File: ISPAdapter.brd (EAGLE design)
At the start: 68 x 38 mm, 5 parts

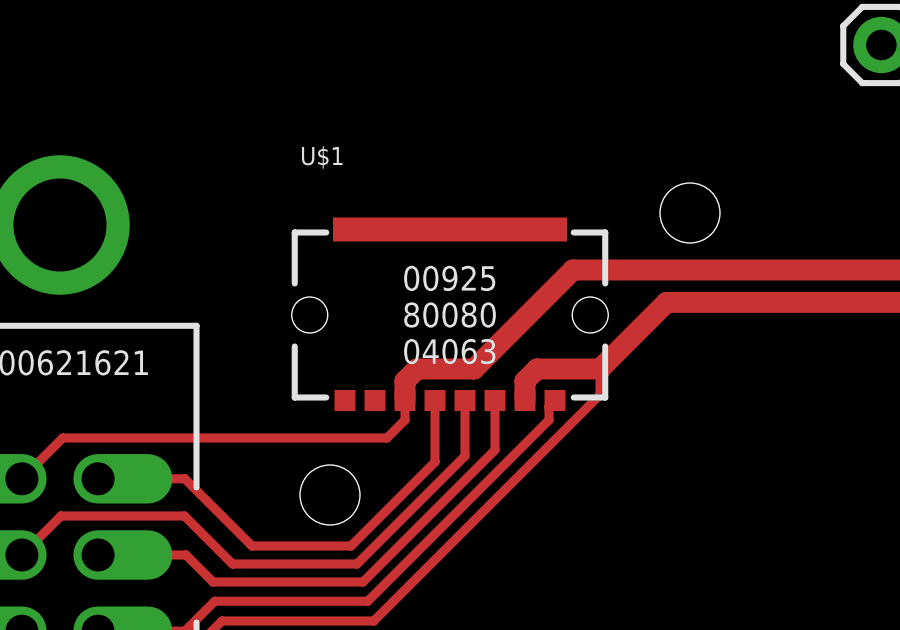
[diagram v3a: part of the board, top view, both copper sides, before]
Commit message: Added PB3 (AUX) to header for HVSP; adjusted LED resistors
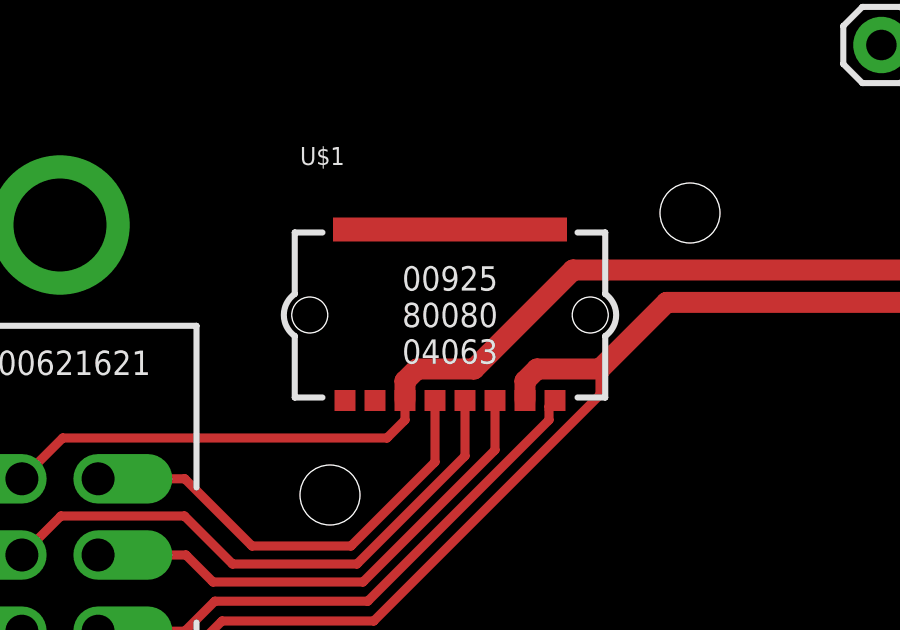
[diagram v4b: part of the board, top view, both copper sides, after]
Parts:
- U$1: device dubec:AVX9258-8P -> dubec:AVX9258-8C
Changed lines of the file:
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@@
 <text x="33.4" y="34" size="1" layer="107" font="vector" ratio="20" rot="SR270" align="center-left">GND</text>
 <text x="7.5" y="1.6" size="0.8128" layer="107" font="vector" ratio="20">201x-xx-xx</text>
-<rectangle x1="15.1" y1="29.45" x2="22.9" y2="30.25" layer="1"/>
 </plain>
 <attributes>
@@
 </element>
 <element name="JP1" library="SparkFun-Connectors" package="1X02" value="M02PTH" x="41" y="36"/>
-<element name="U$1" library="dubec" package="AVX9258-8P" value="AVX9258" x="19" y="27">
+<element name="U$1" library="dubec" package="AVX9258-8C" value="AVX9258" x="19" y="27">
 <attribute name="MANUFACTURER" value="AVX Corporation" x="19" y="27" size="1.778" layer="27" display="off"/>
 <attribute name="EURO" value="1.30" x="19" y="27" size="1.778" layer="27" display="off"/>

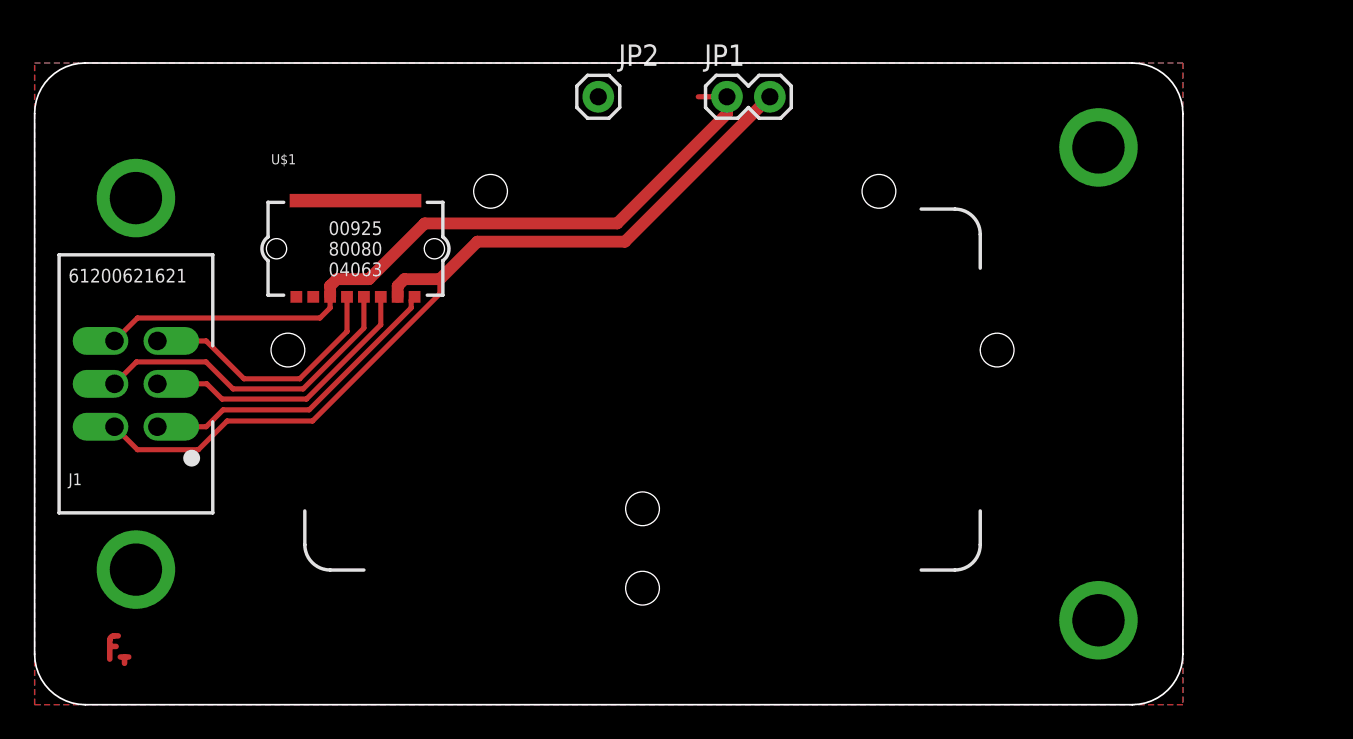
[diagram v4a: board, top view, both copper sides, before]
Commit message: Adapter wiring to match DUBEC 1.5
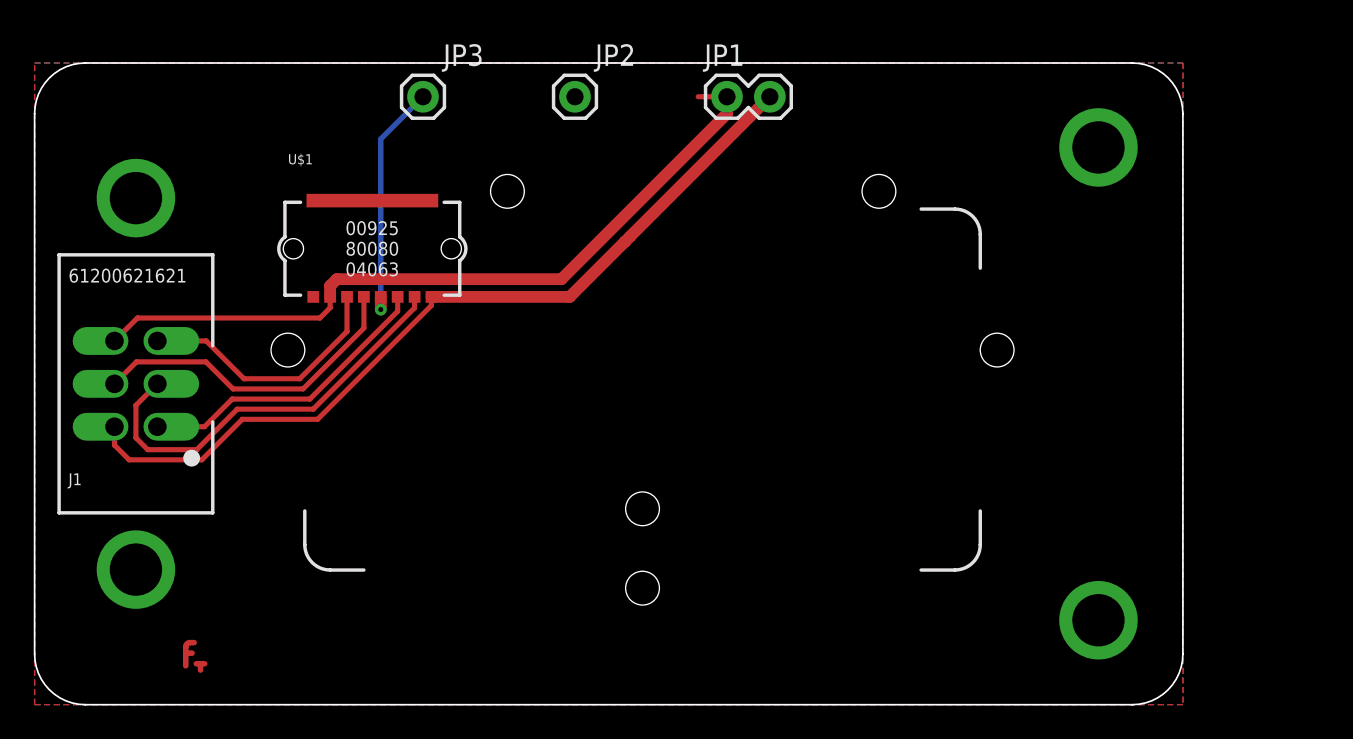
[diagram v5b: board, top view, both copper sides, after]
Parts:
- added JP3: M01PTH, SparkFun-Connectors:1X01
- moved U$2 4.52 mm to (9.50, 2.90)
- moved JP2 1.38 mm to (32.0, 36.0)
- moved U$1 1.00 mm to (20.0, 27.0)
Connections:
- new net AUX: JP3.1, U$1.4
- net DGND: now also U$1.7; no longer U$1.6
- net MISO: now also U$1.3; no longer U$1.1
- net MOSI: now also U$1.5; no longer U$1.4
- net RESET: now also U$1.6; no longer U$1.5
- net SCK: now also U$1.2; no longer U$1.3
- net VCC: now also U$1.1; no longer U$1.2
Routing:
- net AUX: track 0.00 -> 14.4 mm, vias 0 -> 1
- net SCK: track 17.1 -> 24.6 mm
- net VCC: track 51.8 -> 49.5 mm
- net MISO: track 18.7 -> 17.9 mm
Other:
- board text added: "AUX"

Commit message: ISP/DW-switch
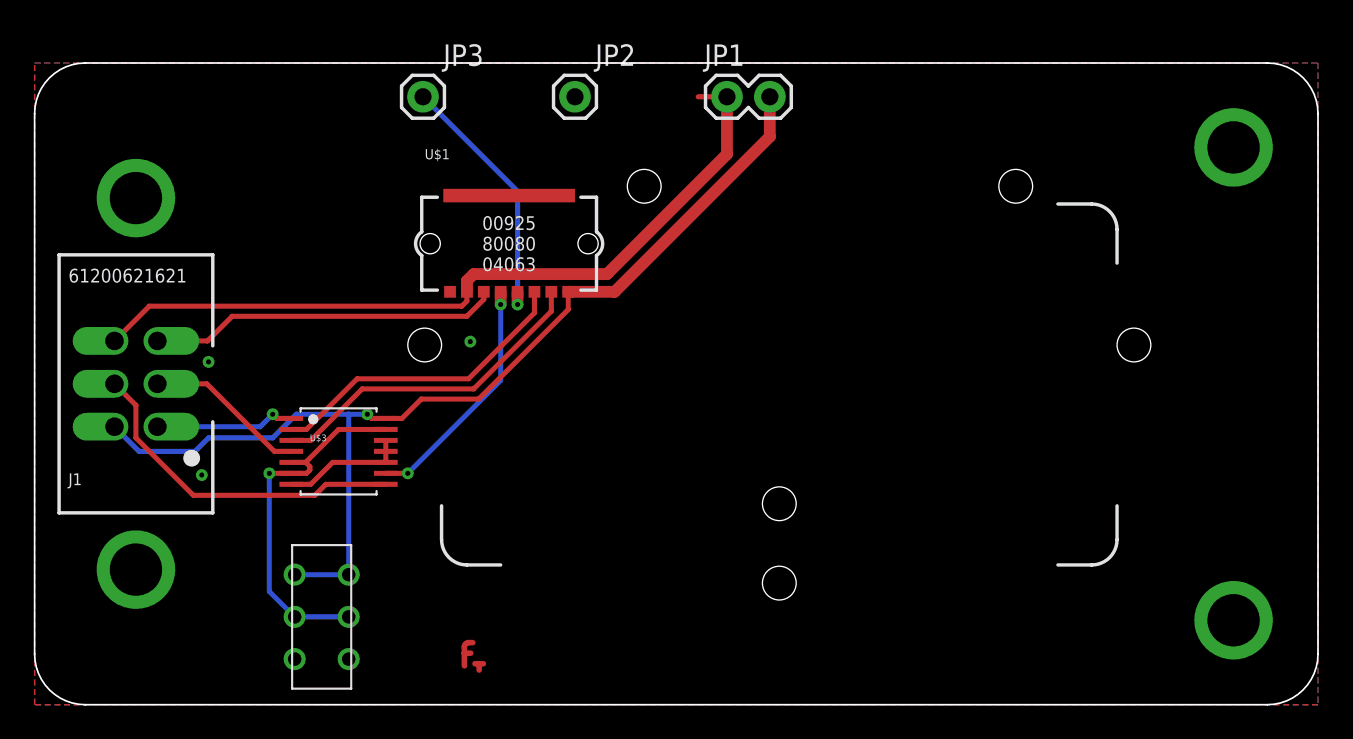
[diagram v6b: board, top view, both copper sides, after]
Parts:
- added S1: (no value), SparkFun-Electromechanical:EG1271A
- added U$3: SWITCH_IC_QUADSN74HC4066PW, dubec:14-TSSOP
- moved U$2 16.5 mm to (26.0, 2.90)
- moved U$1 8.11 mm to (28.1, 27.3)
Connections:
- new net ISP_EN: S1.2, S1.5, U$3.13, U$3.5, U$3.6
- new net MISO_A: J1.1, U$3.1
- new net MOSI_A: J1.4, U$3.8
- new net SCK_A: J1.3, U$3.4
- net GND: now also S1.3, S1.6, U$3.10, U$3.11, U$3.12, U$3.7
- net MISO: now also U$3.2; no longer J1.1
- net MOSI: now also U$3.9; no longer J1.4
- net SCK: now also U$3.3; no longer J1.3
- net VCC: now also S1.1, S1.4, U$3.14
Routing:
- net ISP_EN: track 0.00 -> 21.8 mm, vias 0 -> 1
- net MOSI_A: track 0.00 -> 20.2 mm
- net VCC: track 49.5 -> 63.0 mm, vias 0 -> 1
- net SCK_A: track 0.00 -> 9.59 mm
- net MISO_A: track 0.00 -> 8.34 mm, vias 0 -> 1
- net GND: track 2.40 -> 9.84 mm, vias 4 -> 7
- net RESET: track 15.4 -> 20.8 mm
- net MOSI: track 19.3 -> 14.3 mm, vias 0 -> 2
- net SCK: track 24.6 -> 19.7 mm
- net DGND: track 43.6 -> 45.0 mm
- net AUX: track 14.4 -> 15.4 mm
- net MISO: track 17.9 -> 18.5 mm
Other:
- board size 68 x 38 mm -> 76 x 38 mm
- board text added: "DW"
- board text added: "ISP"

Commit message: Tidy
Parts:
- moved S1 0.20 mm to (17.0, 5.00)
- moved U$1 0.12 mm to (28.2, 27.3)
- renumbered U$3 to U1
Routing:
- net ISP_EN: track 21.8 -> 25.1 mm
- net VCC: track 63.0 -> 66.3 mm
- net GND: track 9.84 -> 9.24 mm
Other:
- board text added: "SPI"
- board text removed: "ISP"

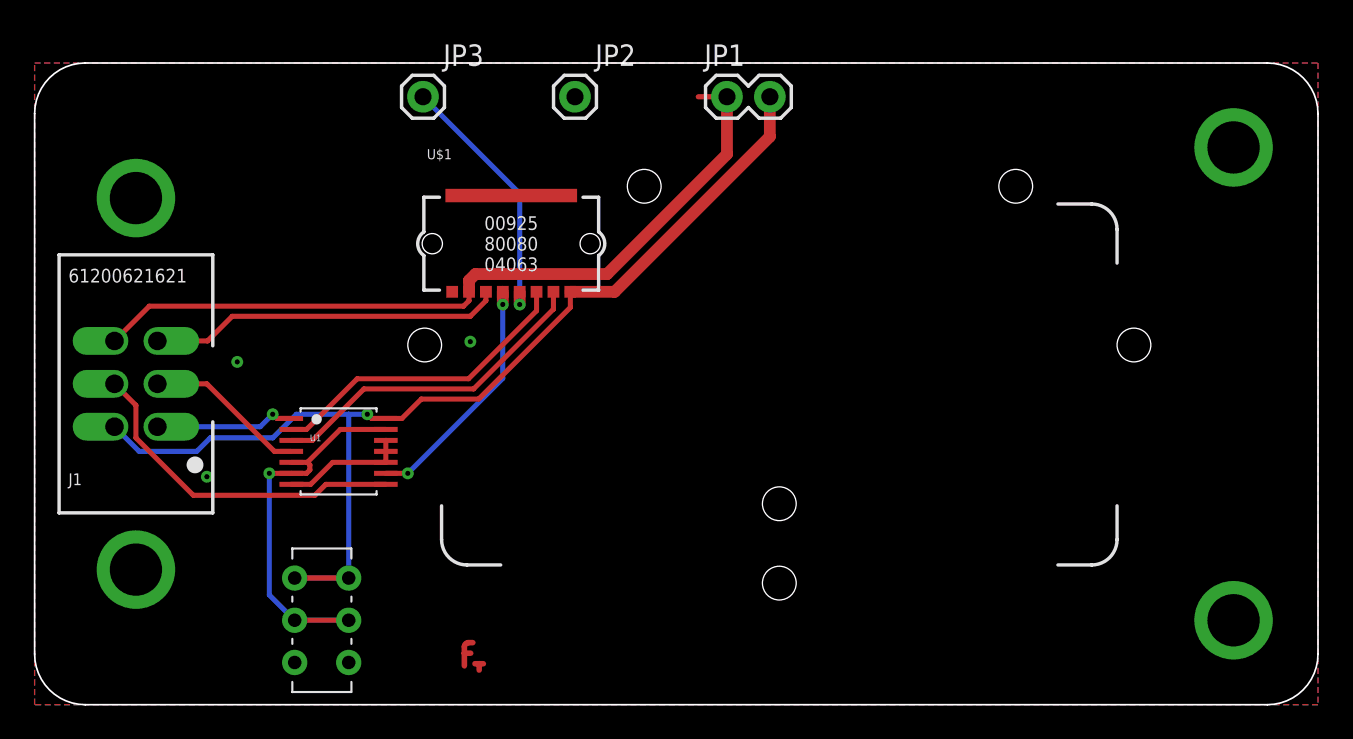
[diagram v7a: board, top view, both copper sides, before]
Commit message: Changed switch IC
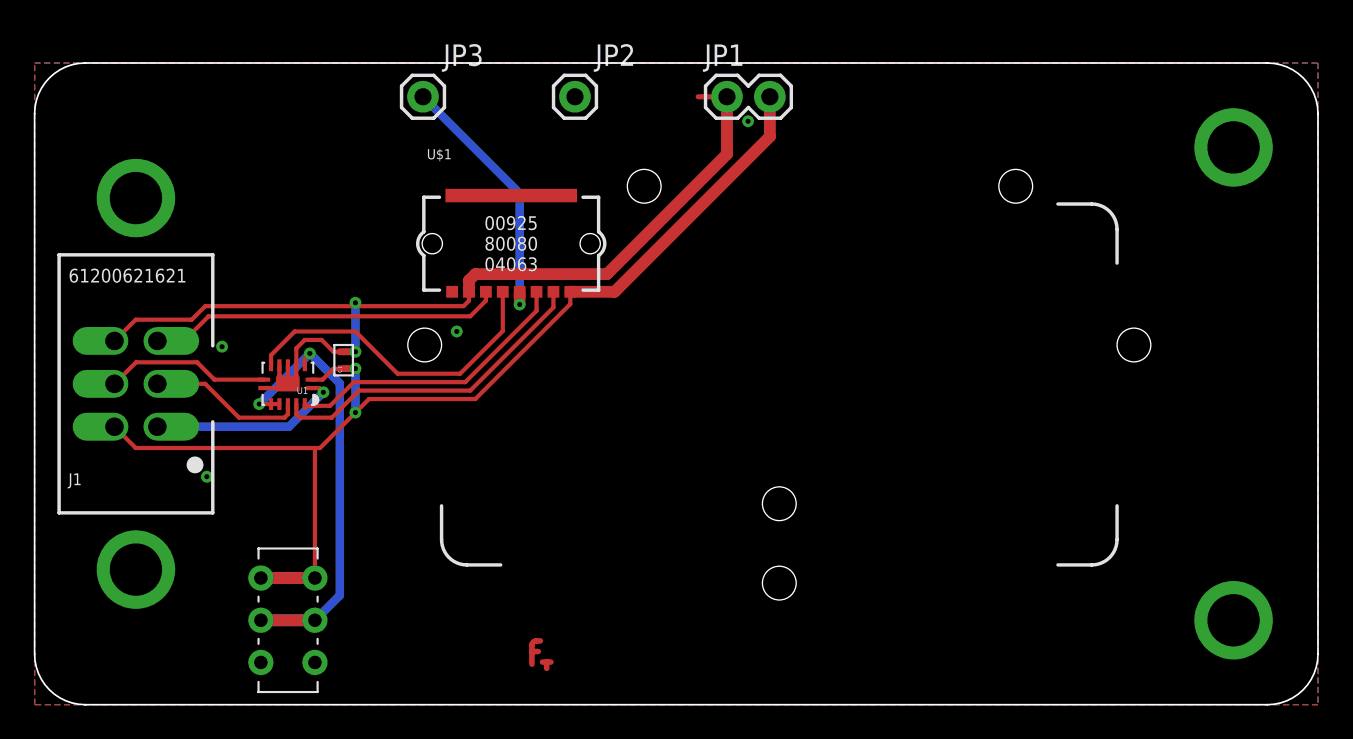
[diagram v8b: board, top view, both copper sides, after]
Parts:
- added C1: (no value), dubec:0402
- U1: value SWITCH_IC_QUADSN74HC4066PW -> SWITCH_IC_QUAD74LVC4066; device dubec:14-TSSOP -> dubec:14-VFQFN
- moved U1 5.00 mm to (15.0, 19.0), turned to 180 degrees
- moved U$2 4.00 mm to (30.0, 3.00)
- moved S1 2.00 mm to (15.0, 5.00)
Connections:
- net DGND: now also C1.2, U1.10, U1.11, U1.12, U1.7, U1.PAD
- net GND: no longer U1.10, U1.11, U1.12, U1.7
- net VCC: now also C1.1
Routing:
- net DGND: track 45.0 -> 58.5 mm, vias 0 -> 2
- net MOSI_A: track 20.2 -> 9.82 mm
- net GND: track 9.24 -> 1.80 mm, vias 7 -> 8
- net MOSI: track 14.4 -> 19.3 mm, vias 2 -> 0
- net ISP_EN: track 25.1 -> 29.8 mm, vias 1 -> 2
- net MISO_A: track 8.34 -> 11.5 mm
- net VCC: track 66.3 -> 69.3 mm, vias 1 -> 2
- net MISO: track 18.6 -> 17.3 mm
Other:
- board text added: "AVR ISP adapter board for Super DUBEC"
- board text added: "Rev. 2 (201x-xx-xx)"
- board text removed: "201x-xx-xx"
- board text removed: "AVR ISP adapter board for Super DUBEC. Rev. 2"
